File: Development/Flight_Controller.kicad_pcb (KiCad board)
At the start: 4 copper layers, 98.7 x 104 mm, 233 parts, among them J1 USB_C_Receptacle, J2 Micro_SD_Card_Det, J3 Conn_01x13_Female, J4 Conn_01x13_Female, J5 Conn_01x13_Female, U1 MIC5330-SPYML, U10 STM32F765IIT6, U11 SN74LVC8T245, U12 TXS0108EPW, U13 NUF2042XV6T1G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

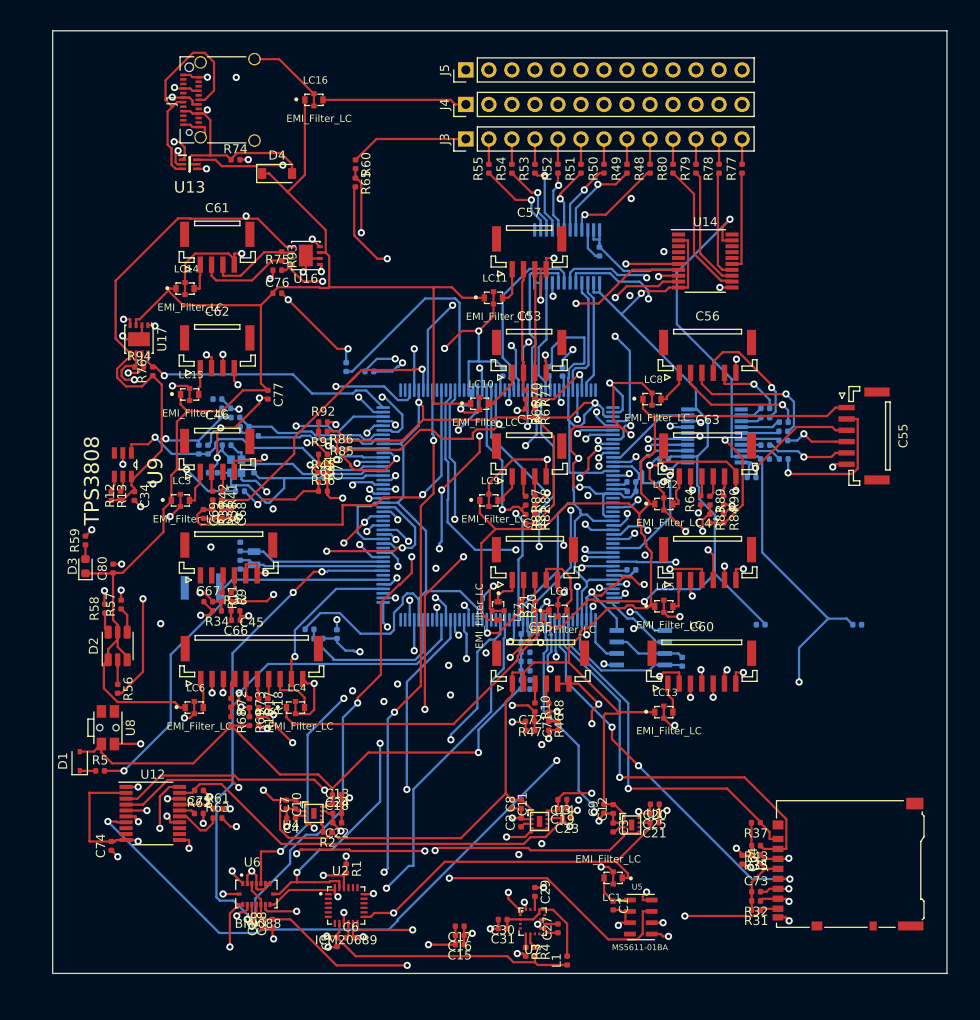
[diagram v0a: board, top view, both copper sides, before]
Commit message: PCB GND Fill fix
Hopefully it doesn't break this time..
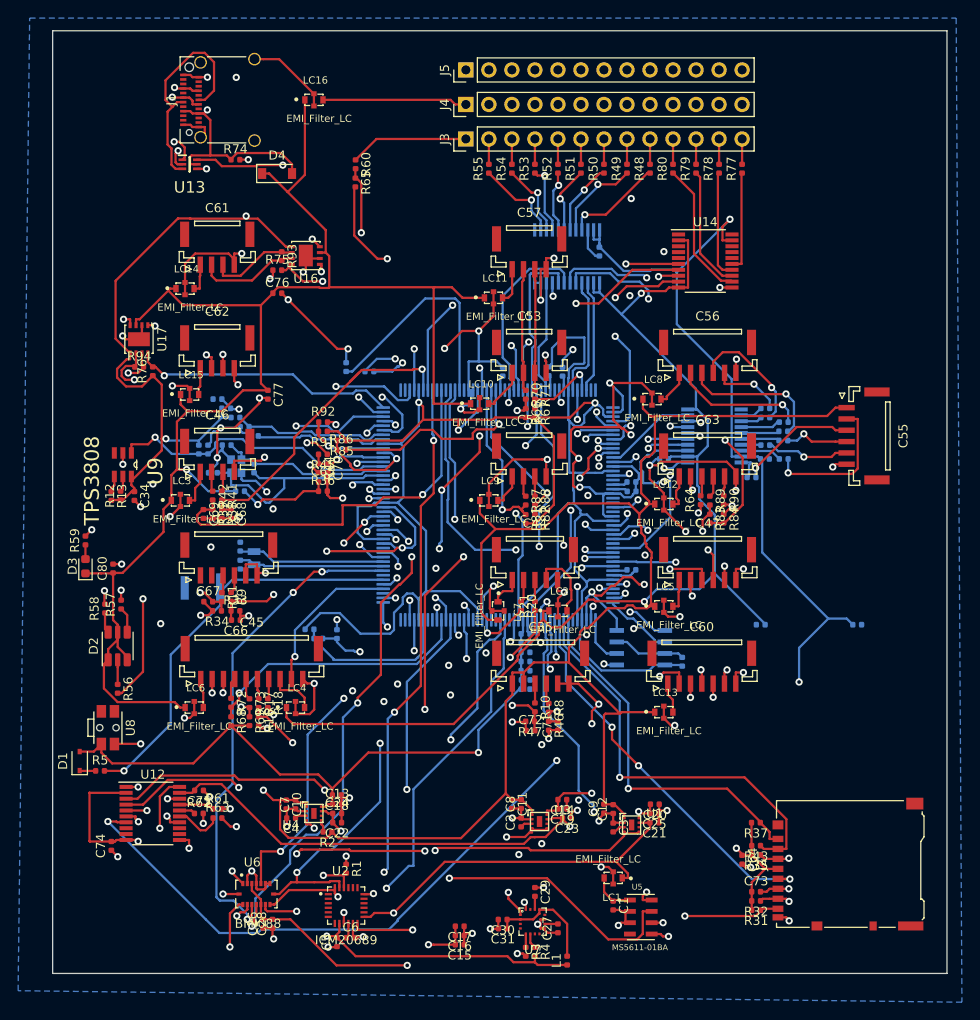
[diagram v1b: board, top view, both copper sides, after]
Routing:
- added copper zone on B.Cu, net GND
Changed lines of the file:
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@@
     (solder_mask_min_width 0.25)
     (aux_axis_origin 0 0)
-    (visible_elements 7FFFFFFF)
+    (visible_elements 7FFFF7FF)
     (pcbplotparams
       (layerselection 0x010fc_ffffffff)
@@
   (via (at 108.2979 126.3844) (size 0.8) (layers F.Cu B.Cu) (net 236))
   (via (at 89.7488 126.1671) (size 0.8) (layers F.Cu B.Cu) (net 236))
+  (zone (net 1) (net_name GND) (layer B.Cu) (hatch edge 0.508)
+    (connect_pads (clearance 0.508))
+    (min_thickness 0.254)
+    (fill yes (arc_segments 32) (thermal_gap 0.508) (thermal_bridge_width 0.508))
+    (polygon
+      (pts
+        (xy 66.675 41.275) (xy 168.91 41.275) (xy 169.545 149.86) (xy 65.405 148.59)
+      )
+    )
+  )
 )

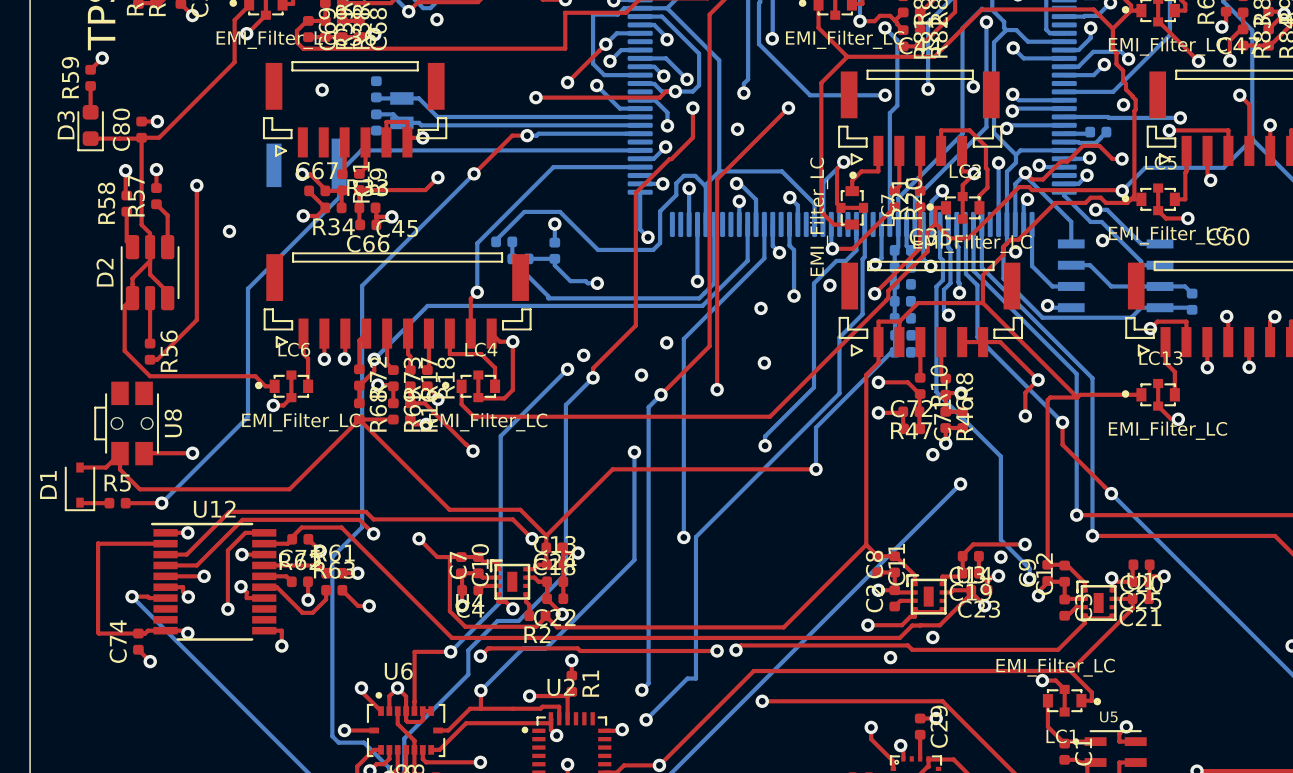
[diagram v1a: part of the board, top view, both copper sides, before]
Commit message: Updated some capacitor footprints
Updated footprints from from 0402_1005 to 0603_1608, still need to do a lot more
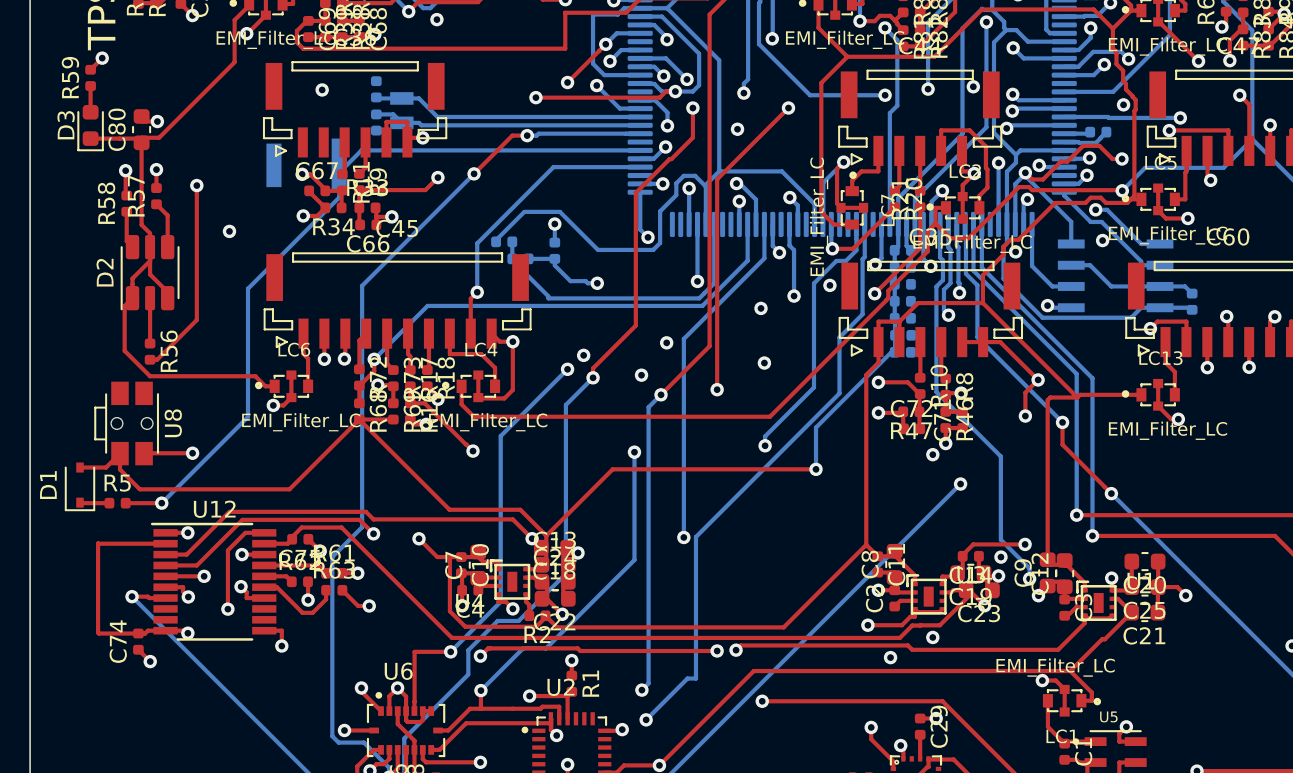
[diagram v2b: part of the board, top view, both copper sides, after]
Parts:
- C12, C13, C18, C19, C20, C21, C22, C23, C24, C25, C7, C8, C80, C9: footprint Capacitor_SMD:C_0402_1005Metric -> Capacitor_SMD:C_0603_1608Metric
- moved C21 0.86 mm to (135.9, 130.9)
- moved C25 0.41 mm to (135.9, 129.3)
- moved C20 0.28 mm to (135.9, 127.8)
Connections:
- C36 pad 1: (no net) -> Net-(C36-Pad1)
- C36 pad 2: (no net) -> Net-(C36-Pad2)
- J1 pad A10: (no net) -> Net-(J1-PadA10)
- J1 pad A11: (no net) -> Net-(J1-PadA11)
- J1 pad A2: (no net) -> Net-(J1-PadA2)
- J1 pad A3: (no net) -> Net-(J1-PadA3)
- J1 pad A5: (no net) -> Net-(J1-PadA5)
- J1 pad A8: (no net) -> Net-(J1-PadA8)
- J1 pad B10: (no net) -> Net-(J1-PadB10)
- J1 pad B11: (no net) -> Net-(J1-PadB11)
- J1 pad B2: (no net) -> Net-(J1-PadB2)
- J1 pad B3: (no net) -> Net-(J1-PadB3)
- J1 pad B5: (no net) -> Net-(J1-PadB5)
- J1 pad B8: (no net) -> Net-(J1-PadB8)
- U1 pad 6: (no net) -> Net-(U1-Pad6)
- U10 pad 105: (no net) -> /SPI5_DRDY7_EXTERNAL1
- U10 pad 109: (no net) -> /VDD_5V_RC_EN
- U10 pad 110: (no net) -> /VDD_5V_WIFI_EN
- U10 pad 112: (no net) -> /USART6_RTS_TELEM3
- U10 pad 119: (no net) -> /CAN3_RX
- U10 pad 13: (no net) -> /SPI5_CS3_EXTERNAL1
- U10 pad 130: (no net) -> /SPI5_SYNC_EXTERNAL1
- U10 pad 138: (no net) -> /CAN3_TX
- U10 pad 152: (no net) -> /USART6_RX_TELEM3
- U10 pad 155: (no net) -> /SPI6_MISO_EXTERNAL2
- U10 pad 156: (no net) -> /SPI6_SCK_EXTERNAL2
- U10 pad 160: (no net) -> /USART6_CTS_TELEM3
- U10 pad 163: (no net) -> /SPI6_MOSI_EXTERNAL2
- U10 pad 169: (no net) -> /UART8_RX
- U10 pad 170: (no net) -> /UART8_TX
- U10 pad 175: (no net) -> /SPI6_CS1_EXTERNAL2
- U10 pad 176: (no net) -> /SPI6_CS2_EXTERNAL2
- U10 pad 19: (no net) -> /SPI1_CS2_ICM20602
- U10 pad 3: (no net) -> /VDD_3V3_SPEKTRUM_POWER_EN
- U10 pad 45: (no net) -> /CAN3_SILENT_S2
- U10 pad 46: (no net) -> /SPI1_CS5_AUX_MEM
- U10 pad 53: (no net) -> /HEATER
- U10 pad 55: (no net) -> /SPI1_DRDY4_ICM20602
- U10 pad 59: (no net) -> /SPI4_CS2
- U10 pad 68: (no net) -> /DRDY8
- U10 pad 7: (no net) -> /SPI6_CS3_EXTERNAL2
- U10 pad 79: (no net) -> /nSPI5_RESET_EXTERNAL1
- U10 pad 87: (no net) -> /[n]UI_LED_RED[_EXTERNAL]
- U10 pad 88: (no net) -> /[n]UI_LED_GREEN[_EXTERNAL]
- U10 pad 89: (no net) -> /[n]UI_LED_BLUE[_EXTERNAL]
- U12 pad 12: (no net) -> Net-(U12-Pad12)
- U12 pad 13: (no net) -> Net-(U12-Pad13)
- U12 pad 8: (no net) -> Net-(U12-Pad8)
- U12 pad 9: (no net) -> Net-(U12-Pad9)
- U14 pad 1: (no net) -> Net-(U14-Pad1)
- U14 pad 16: (no net) -> Net-(U14-Pad16)
- U14 pad 17: (no net) -> Net-(U14-Pad17)
- U14 pad 18: (no net) -> Net-(U14-Pad18)
- U14 pad 20: (no net) -> Net-(U14-Pad20)
- U14 pad 3: (no net) -> Net-(U14-Pad3)
- U14 pad 4: (no net) -> Net-(U14-Pad4)
- U14 pad 5: (no net) -> Net-(U14-Pad5)
- U2 pad 1: (no net) -> Net-(U2-Pad1)
- U2 pad 14: (no net) -> Net-(U2-Pad14)
- U2 pad 15: (no net) -> Net-(U2-Pad15)
- U2 pad 16: (no net) -> Net-(U2-Pad16)
- U2 pad 17: (no net) -> Net-(U2-Pad17)
- U2 pad 19: (no net) -> Net-(U2-Pad19)
- U2 pad 2: (no net) -> Net-(U2-Pad2)
- U2 pad 20: (no net) -> Net-(U2-Pad20)
- U2 pad 21: (no net) -> Net-(U2-Pad21)
- U2 pad 3: (no net) -> Net-(U2-Pad3)
- U2 pad 4: (no net) -> Net-(U2-Pad4)
- U2 pad 5: (no net) -> Net-(U2-Pad5)
- U2 pad 6: (no net) -> Net-(U2-Pad6)
- U2 pad 7: (no net) -> Net-(U2-Pad7)
- U3 pad 6: (no net) -> Net-(U3-Pad6)
- U4 pad 6: (no net) -> Net-(U4-Pad6)
- U5 pad 4: (no net) -> Net-(U5-Pad4)
- U7 pad 12: (no net) -> Net-(U7-Pad12)
- U7 pad 15: (no net) -> Net-(U7-Pad15)
- U7 pad 3: (no net) -> Net-(U7-Pad3)
- U7 pad 4: (no net) -> Net-(U7-Pad4)
- U7 pad 7: (no net) -> Net-(U7-Pad7)
- U7 pad 8: (no net) -> Net-(U7-Pad8)
- U8 pad 1: (no net) -> Net-(U8-Pad1)
- U8 pad 3: (no net) -> Net-(U8-Pad3)
- U9 pad 3: (no net) -> Net-(U9-Pad3)
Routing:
- net GND: track 526.6 -> 528.6 mm
- net IMU_3V3: track 131.7 -> 132.2 mm

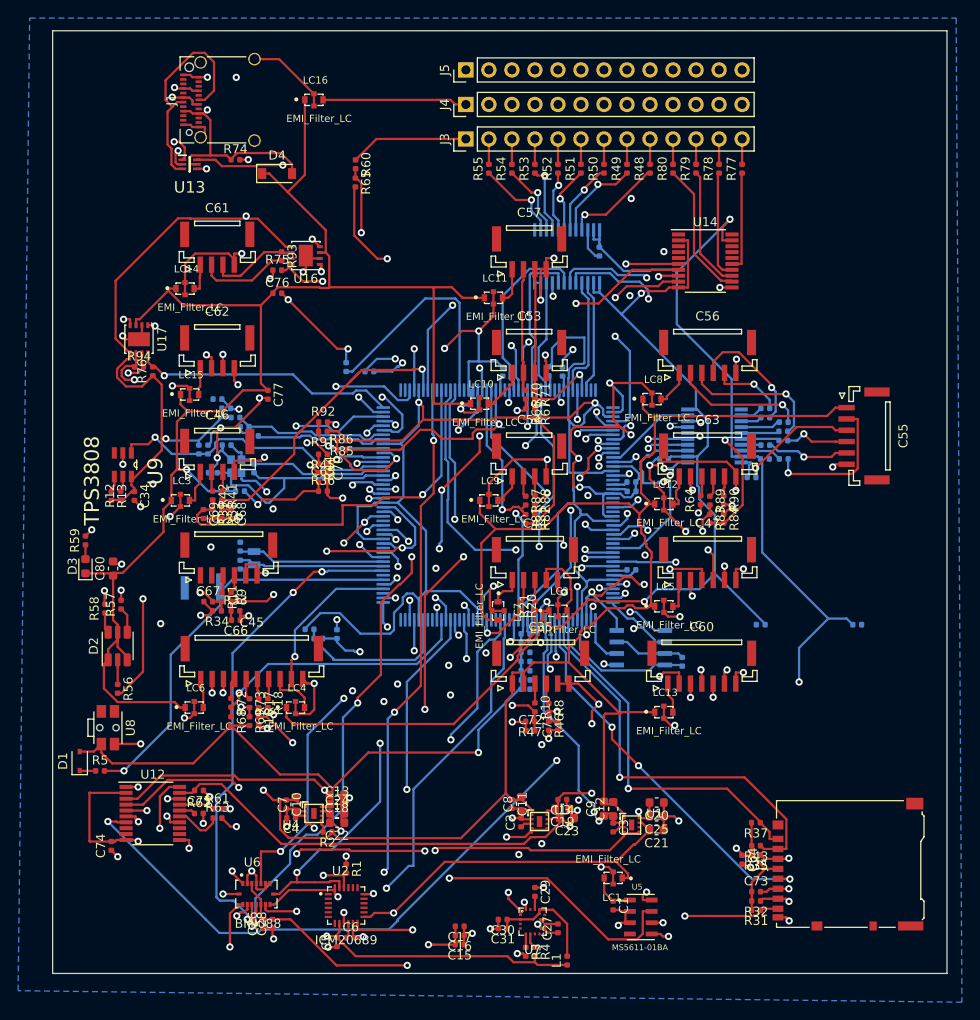
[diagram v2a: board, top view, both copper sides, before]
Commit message: Completely updated capacitor footprints
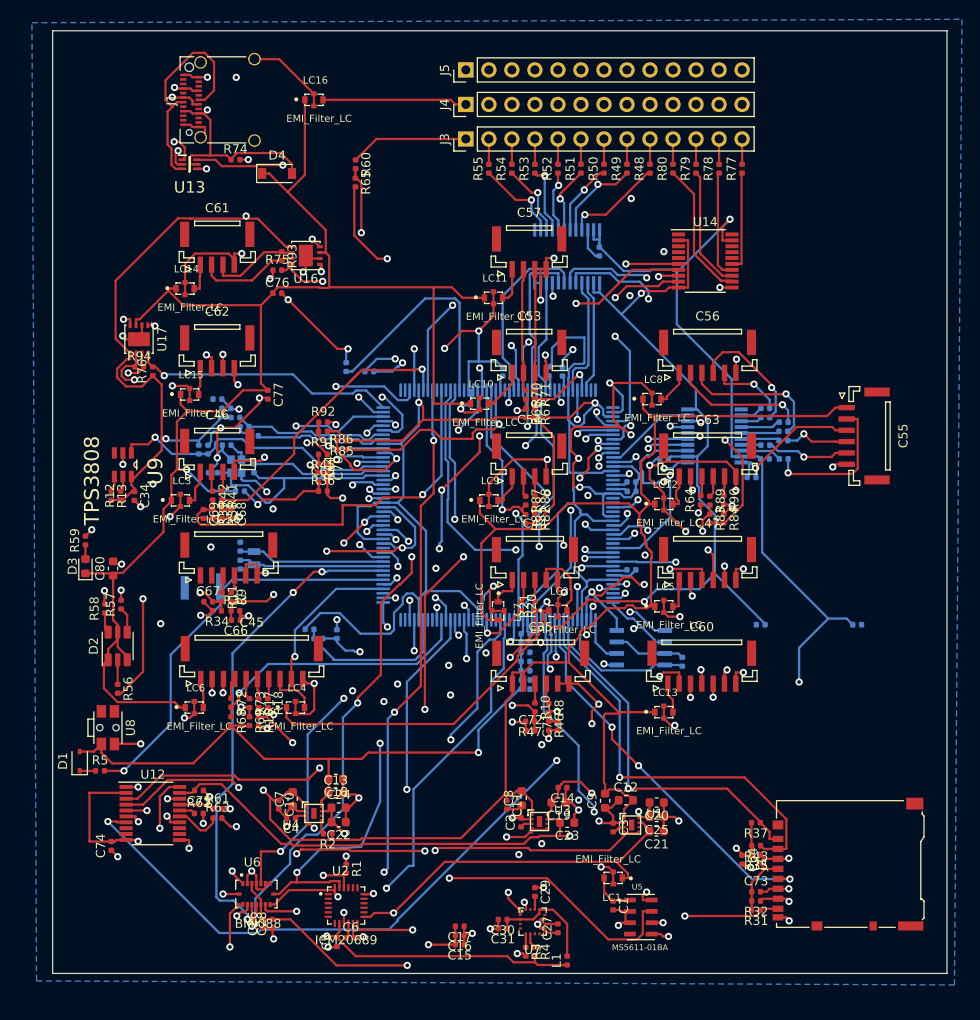
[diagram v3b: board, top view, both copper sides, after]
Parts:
- moved C18 1.78 mm to (100.5, 125.2)
- moved C12 1.70 mm to (132.5, 127.6), turned to 0 degrees
- moved C14 1.33 mm to (125.5, 126.2)
- moved C13 1.22 mm to (100.5, 126.8)
- moved C9 0.88 mm to (130.2, 127.6)
- moved C10 0.83 mm to (94.2, 128.1)
- moved C19 0.82 mm to (125.0, 127.8)
- moved C7 0.67 mm to (95.7, 127.4)
- moved C24 0.66 mm to (100.8, 128.4)
- moved C8 0.65 mm to (121.0, 127.3)
- moved C11 0.58 mm to (119.3, 128.1)
- moved C23 0.51 mm to (126.0, 130.0)
- moved R2 0.19 mm to (99.6, 131.3)
- moved C22 0.18 mm to (100.8, 130.0)
- moved C21 0.13 mm to (135.9, 131.0)
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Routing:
- net GND: track 528.6 -> 539.7 mm
- net VCC: track 392.6 -> 397.6 mm
- net D2_3V3: track 165.6 -> 167.6 mm
- net TF_3V3: track 65.3 -> 67.1 mm
- net IO1_3V3: track 224.2 -> 225.4 mm
- net SPI1_SCK_SENSOR1: track 52.3 -> 53.4 mm
- net SPI1_CS1_ICM20689: track 46.5 -> 47.6 mm
- net UART7_RX_DEBUG: track 59.7 -> 58.8 mm

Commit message: Fixed all PCB errors
Ready to print!
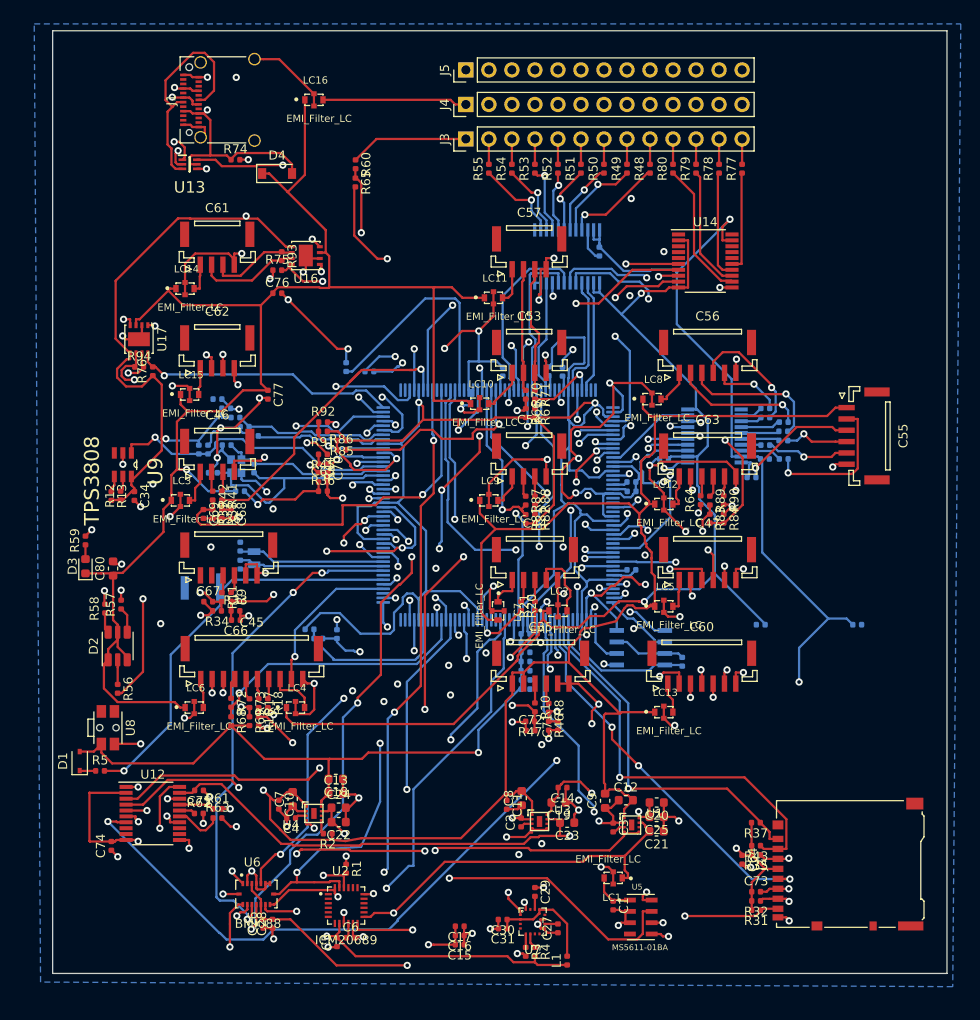
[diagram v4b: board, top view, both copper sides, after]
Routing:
- net MCU_3V3: track 465.2 -> 470.2 mm
- net SPI1_DRDY3_BMI055_ACC: track 93.8 -> 97.1 mm
- net SPI1_DRDY6_BMI055_ACC: track 87.1 -> 84.4 mm
- net USART2_CTS_TELEM1: track 30.7 -> 31.6 mm
- net I2C_3_SDA_PORT: track 13.4 -> 14.2 mm
- net SPI1_DRDY2_BMI055_GYRO: track 84.2 -> 84.8 mm
- net nLED_BLUE: track 68.8 -> 69.4 mm
- net USART3_CTS_TELEM2: track 16.2 -> 16.7 mm
- net USART3_RX_TELEM2: track 19.9 -> 20.4 mm
- net GND: track 539.7 -> 539.5 mm, vias 91 -> 90
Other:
- rule trace_min: 0.1 -> 0.2
- rule via_min_size: 0.1 -> 0.4
